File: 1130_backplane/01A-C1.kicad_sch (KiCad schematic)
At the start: 86 parts

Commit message: Removed power rails off 01A-C1 N2 connector
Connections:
- net +3V: no longer J253.b2 (Pin_b2)
- net +6V: no longer J253.a10 (Pin_a10)
- net -3V: no longer J253.a5 (Pin_a5)
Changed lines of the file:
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@@
     (stroke (width 0) (type solid) (color 0 0 0 0))
-  )
-  (wire (pts (xy 538.48 127) (xy 546.1 127))
-    (stroke (width 0) (type default) (color 0 0 0 0))
   )
   (wire (pts (xy 306.07 119.38) (xy 314.96 119.38))
@@
     (stroke (width 0) (type default) (color 0 0 0 0))
   )
-  (wire (pts (xy 558.8 106.68) (xy 566.42 106.68))
-    (stroke (width 0) (type default) (color 0 0 0 0))
-  )
   (polyline (pts (xy 196.85 33.02) (xy 198.12 33.02))
     (stroke (width 0) (type solid) (color 0 0 0 0))
@@
     (stroke (width 0) (type default) (color 0 0 0 0))
   )
-  (wire (pts (xy 538.48 114.3) (xy 546.1 114.3))
-    (stroke (width 0) (type default) (color 0 0 0 0))
-  )
   (wire (pts (xy 160.02 152.4) (xy 167.64 152.4))
     (stroke (width 0) (type default) (color 0 0 0 0))
@@
     (effects (font (size 1.27 1.27)) (justify right bottom))
   )
-  (label "-3V" (at 538.48 114.3 180)
-    (effects (font (size 1.27 1.27)) (justify right bottom))
-  )
   (label "+3V" (at 440.69 144.78 0)
     (effects (font (size 1.27 1.27)) (justify left bottom))
@@
     (effects (font (size 1.27 1.27)) (justify right bottom))
   )
-  (label "+3V" (at 566.42 106.68 0)
-    (effects (font (size 1.27 1.27)) (justify left bottom))
-  )
   (label "+3V" (at 482.6 182.88 0)
     (effects (font (size 1.27 1.27)) (justify left bottom))
@@
     (effects (font (size 1.27 1.27)) (justify left bottom))
   )
-  (label "+6V" (at 538.48 127 180)
-    (effects (font (size 1.27 1.27)) (justify right bottom))
-  )
   (label "-3V" (at 160.02 266.7 180)

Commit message: DN101-DN111 added to backplane schematics, DN111 01B-A1 connections made, 01B-B1 connections to be made when all signals on connectors
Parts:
- removed J173, J174, J175, J176, J177, J178, J179, J180, J181, J182, J183, J184, J185, J186, J187, J188, J189, J190, J191, J192, J193, J194, J195, J196, J197, J198, J199, J200, J201, J202, J203, J204, J205, J206, J207, J208, J209, J210, J211, J212, J213, J214, J215, J216, J217, J218, J219, J220, J221, J222, J223, J224, J225, J226, J227, J228, J229, J230, J231, J232, J233, J234, J235, J236, J237, J238, J239, J240, J241, J242, J243, J244, J245, J246, J247, J248, J249, J250, J251, J252, J253, J254, J255, J256, J257, J258: ~, symbol Connector_Generic:Conn_02x12_Row_Letter_First
- added J? (x86): ~, symbol Connector_Generic:Conn_02x12_Row_Letter_First
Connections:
- net +3V: now also J?.b2 (Pin_b2), J?.b2 (Pin_b2), J?.b2 (Pin_b2), J?.b2 (Pin_b2), J?.b2 (Pin_b2), J?.b2 (Pin_b2), J?.b2 (Pin_b2), J?.b2 (Pin_b2), J?.b2 (Pin_b2), J?.b2 (Pin_b2), J?.b2 (Pin_b2), J?.b2 (Pin_b2), J?.b2 (Pin_b2), J?.b2 (Pin_b2), J?.b2 (Pin_b2), J?.b2 (Pin_b2), J?.b2 (Pin_b2), J?.b2 (Pin_b2), J?.b2 (Pin_b2), J?.b2 (Pin_b2), J?.b2 (Pin_b2), J?.b2 (Pin_b2), J?.b2 (Pin_b2), J?.b2 (Pin_b2), J?.b2 (Pin_b2), J?.b2 (Pin_b2), J?.b2 (Pin_b2), J?.b2 (Pin_b2), J?.b2 (Pin_b2), J?.b2 (Pin_b2), J?.b2 (Pin_b2), J?.b2 (Pin_b2), J?.b2 (Pin_b2), J?.b2 (Pin_b2), J?.b2 (Pin_b2), J?.b2 (Pin_b2), J?.b2 (Pin_b2), J?.b2 (Pin_b2), J?.b2 (Pin_b2), J?.b2 (Pin_b2), J?.b2 (Pin_b2), J?.b2 (Pin_b2), J?.b2 (Pin_b2), J?.b2 (Pin_b2), J?.b2 (Pin_b2), J?.b2 (Pin_b2), J?.b2 (Pin_b2), J?.b2 (Pin_b2), J?.b2 (Pin_b2), J?.b2 (Pin_b2), J?.b2 (Pin_b2), J?.b2 (Pin_b2), J?.b2 (Pin_b2), J?.b2 (Pin_b2), J?.b2 (Pin_b2), J?.b2 (Pin_b2), J?.b2 (Pin_b2), J?.b2 (Pin_b2), J?.b2 (Pin_b2), J?.b2 (Pin_b2), J?.b2 (Pin_b2), J?.b2 (Pin_b2), J?.b2 (Pin_b2), J?.b2 (Pin_b2), J?.b2 (Pin_b2), J?.b2 (Pin_b2), J?.b2 (Pin_b2), J?.b2 (Pin_b2), J?.b2 (Pin_b2), J?.b2 (Pin_b2), J?.b2 (Pin_b2), J?.b2 (Pin_b2), J?.b2 (Pin_b2), J?.b2 (Pin_b2), J?.b2 (Pin_b2), J?.b2 (Pin_b2), J?.b2 (Pin_b2)
- net +6V: now also J?.a10 (Pin_a10), J?.a10 (Pin_a10), J?.a10 (Pin_a10), J?.a10 (Pin_a10), J?.a10 (Pin_a10), J?.a10 (Pin_a10), J?.a10 (Pin_a10), J?.a10 (Pin_a10), J?.a10 (Pin_a10), J?.a10 (Pin_a10), J?.a10 (Pin_a10), J?.a10 (Pin_a10), J?.a10 (Pin_a10), J?.a10 (Pin_a10), J?.a10 (Pin_a10), J?.a10 (Pin_a10), J?.a10 (Pin_a10), J?.a10 (Pin_a10), J?.a10 (Pin_a10), J?.a10 (Pin_a10), J?.a10 (Pin_a10), J?.a10 (Pin_a10), J?.a10 (Pin_a10), J?.a10 (Pin_a10), J?.a10 (Pin_a10), J?.a10 (Pin_a10), J?.a10 (Pin_a10), J?.a10 (Pin_a10), J?.a10 (Pin_a10), J?.a10 (Pin_a10), J?.a10 (Pin_a10), J?.a10 (Pin_a10), J?.a10 (Pin_a10), J?.a10 (Pin_a10), J?.a10 (Pin_a10), J?.a10 (Pin_a10), J?.a10 (Pin_a10), J?.a10 (Pin_a10), J?.a10 (Pin_a10), J?.a10 (Pin_a10), J?.a10 (Pin_a10), J?.a10 (Pin_a10), J?.a10 (Pin_a10), J?.a10 (Pin_a10), J?.a10 (Pin_a10), J?.a10 (Pin_a10), J?.a10 (Pin_a10), J?.a10 (Pin_a10), J?.a10 (Pin_a10), J?.a10 (Pin_a10), J?.a10 (Pin_a10), J?.a10 (Pin_a10), J?.a10 (Pin_a10), J?.a10 (Pin_a10), J?.a10 (Pin_a10), J?.a10 (Pin_a10), J?.a10 (Pin_a10), J?.a10 (Pin_a10), J?.a10 (Pin_a10), J?.a10 (Pin_a10), J?.a10 (Pin_a10), J?.a10 (Pin_a10), J?.a10 (Pin_a10), J?.a10 (Pin_a10), J?.a10 (Pin_a10), J?.a10 (Pin_a10), J?.a10 (Pin_a10), J?.a10 (Pin_a10), J?.a10 (Pin_a10), J?.a10 (Pin_a10), J?.a10 (Pin_a10), J?.a10 (Pin_a10), J?.a10 (Pin_a10), J?.a10 (Pin_a10), J?.a10 (Pin_a10), J?.a10 (Pin_a10), J?.a10 (Pin_a10)
- net -3V: now also J?.a5 (Pin_a5), J?.a5 (Pin_a5), J?.a5 (Pin_a5), J?.a5 (Pin_a5), J?.a5 (Pin_a5), J?.a5 (Pin_a5), J?.a5 (Pin_a5), J?.a5 (Pin_a5), J?.a5 (Pin_a5), J?.a5 (Pin_a5), J?.a5 (Pin_a5), J?.a5 (Pin_a5), J?.a5 (Pin_a5), J?.a5 (Pin_a5), J?.a5 (Pin_a5), J?.a5 (Pin_a5), J?.a5 (Pin_a5), J?.a5 (Pin_a5), J?.a5 (Pin_a5), J?.a5 (Pin_a5), J?.a5 (Pin_a5), J?.a5 (Pin_a5), J?.a5 (Pin_a5), J?.a5 (Pin_a5), J?.a5 (Pin_a5), J?.a5 (Pin_a5), J?.a5 (Pin_a5), J?.a5 (Pin_a5), J?.a5 (Pin_a5), J?.a5 (Pin_a5), J?.a5 (Pin_a5), J?.a5 (Pin_a5), J?.a5 (Pin_a5), J?.a5 (Pin_a5), J?.a5 (Pin_a5), J?.a5 (Pin_a5), J?.a5 (Pin_a5), J?.a5 (Pin_a5), J?.a5 (Pin_a5), J?.a5 (Pin_a5), J?.a5 (Pin_a5), J?.a5 (Pin_a5), J?.a5 (Pin_a5), J?.a5 (Pin_a5), J?.a5 (Pin_a5), J?.a5 (Pin_a5), J?.a5 (Pin_a5), J?.a5 (Pin_a5), J?.a5 (Pin_a5), J?.a5 (Pin_a5), J?.a5 (Pin_a5), J?.a5 (Pin_a5), J?.a5 (Pin_a5), J?.a5 (Pin_a5), J?.a5 (Pin_a5), J?.a5 (Pin_a5), J?.a5 (Pin_a5), J?.a5 (Pin_a5), J?.a5 (Pin_a5), J?.a5 (Pin_a5), J?.a5 (Pin_a5), J?.a5 (Pin_a5), J?.a5 (Pin_a5), J?.a5 (Pin_a5), J?.a5 (Pin_a5), J?.a5 (Pin_a5), J?.a5 (Pin_a5), J?.a5 (Pin_a5), J?.a5 (Pin_a5), J?.a5 (Pin_a5), J?.a5 (Pin_a5), J?.a5 (Pin_a5), J?.a5 (Pin_a5), J?.a5 (Pin_a5), J?.a5 (Pin_a5), J?.a5 (Pin_a5), J?.a5 (Pin_a5)
- net -IO_BIT_0: now also J?.a1 (Pin_a1), J?.a2 (Pin_a2)
- net -IO_BIT_1: now also J?.b1 (Pin_b1), J?.b1 (Pin_b1)
- net -IO_BIT_10: now also J?.a7 (Pin_a7), J?.a7 (Pin_a7)
- net -IO_BIT_11: now also J?.b6 (Pin_b6), J?.b8 (Pin_b8)
- net -IO_BIT_12: now also J?.a8 (Pin_a8), J?.a8 (Pin_a8)
- net -IO_BIT_13: now also J?.b8 (Pin_b8), J?.b9 (Pin_b9)
- net -IO_BIT_14: now also J?.a9 (Pin_a9), J?.a9 (Pin_a9)
- net -IO_BIT_15: now also J?.b10 (Pin_b10), J?.b9 (Pin_b9)
- net -IO_BIT_2: now also J?.a2 (Pin_a2), J?.a3 (Pin_a3)
- net -IO_BIT_3: now also J?.a1 (Pin_a1), J?.b2 (Pin_b2), J?.b3 (Pin_b3)
- net -IO_BIT_4: now also J?.a3 (Pin_a3), J?.a4 (Pin_a4)
- net -IO_BIT_5: now also J?.b3 (Pin_b3), J?.b4 (Pin_b4)
- net -IO_BIT_6: now also J?.a11 (Pin_a11), J?.a4 (Pin_a4), J?.a5 (Pin_a5)
- net -IO_BIT_7: now also J?.b4 (Pin_b4), J?.b5 (Pin_b5)
- net -IO_BIT_8: now also J?.a6 (Pin_a6), J?.a6 (Pin_a6)
- net -IO_BIT_9: now also J?.b5 (Pin_b5), J?.b6 (Pin_b6)
- net GND: now also J?.b7 (Pin_b7), J?.b7 (Pin_b7), J?.b7 (Pin_b7), J?.b7 (Pin_b7), J?.b7 (Pin_b7), J?.b7 (Pin_b7), J?.b7 (Pin_b7), J?.b7 (Pin_b7), J?.b7 (Pin_b7), J?.b7 (Pin_b7), J?.b7 (Pin_b7), J?.b7 (Pin_b7), J?.b7 (Pin_b7), J?.b7 (Pin_b7), J?.b7 (Pin_b7), J?.b7 (Pin_b7), J?.b7 (Pin_b7), J?.b7 (Pin_b7), J?.b7 (Pin_b7), J?.b7 (Pin_b7), J?.b7 (Pin_b7), J?.b7 (Pin_b7), J?.b7 (Pin_b7), J?.b7 (Pin_b7), J?.b7 (Pin_b7), J?.b7 (Pin_b7), J?.b7 (Pin_b7), J?.b7 (Pin_b7), J?.b7 (Pin_b7), J?.b7 (Pin_b7), J?.b7 (Pin_b7), J?.b7 (Pin_b7), J?.b7 (Pin_b7), J?.b7 (Pin_b7), J?.b7 (Pin_b7), J?.b7 (Pin_b7), J?.b7 (Pin_b7), J?.b7 (Pin_b7), J?.b7 (Pin_b7), J?.b7 (Pin_b7), J?.b7 (Pin_b7), J?.b7 (Pin_b7), J?.b7 (Pin_b7), J?.b7 (Pin_b7), J?.b7 (Pin_b7), J?.b7 (Pin_b7), J?.b7 (Pin_b7), J?.b7 (Pin_b7), J?.b7 (Pin_b7), J?.b7 (Pin_b7), J?.b7 (Pin_b7), J?.b7 (Pin_b7), J?.b7 (Pin_b7), J?.b7 (Pin_b7), J?.b7 (Pin_b7), J?.b7 (Pin_b7), J?.b7 (Pin_b7), J?.b7 (Pin_b7), J?.b7 (Pin_b7), J?.b7 (Pin_b7), J?.b7 (Pin_b7), J?.b7 (Pin_b7), J?.b7 (Pin_b7), J?.b7 (Pin_b7), J?.b7 (Pin_b7), J?.b7 (Pin_b7), J?.b7 (Pin_b7), J?.b7 (Pin_b7), J?.b7 (Pin_b7), J?.b7 (Pin_b7), J?.b7 (Pin_b7), J?.b7 (Pin_b7), J?.b7 (Pin_b7), J?.b7 (Pin_b7), J?.b7 (Pin_b7), J?.b7 (Pin_b7), J?.b7 (Pin_b7), J?.b7 (Pin_b7), J?.b7 (Pin_b7), J?.b7 (Pin_b7), J?.b7 (Pin_b7), J?.b7 (Pin_b7), J?.b7 (Pin_b7), J?.b7 (Pin_b7), J?.b7 (Pin_b7), J?.b7 (Pin_b7)

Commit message: Add labels for cable runs, completed tracing for DN111 from previous commit, decided it would be too much work to go back and route later... Completed DN201 page.
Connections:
- net +3V: no longer J?.b2 (Pin_b2), J?.b2 (Pin_b2), J?.b2 (Pin_b2)
- net +6V: no longer J?.a10 (Pin_a10), J?.a10 (Pin_a10), J?.a10 (Pin_a10)
- net -3V: no longer J?.a5 (Pin_a5), J?.a5 (Pin_a5), J?.a5 (Pin_a5)
- net +INT_RUN_MODE: now reaches J?.a4 (Pin_a4)
- net +INT_RUN_MODE: now also J?.a4 (Pin_a4), J?.b6 (Pin_b6)
- net -XIO_TIME_GATE: now reaches J?.a3 (Pin_a3)
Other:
- note added: "CABL 01A-B1T1"
- note added: "CABL 01B-A1A6"
- note added: "CABL 01B-A1A7"
- note added: "CABL 01B-B1N5"
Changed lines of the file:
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@@
     (stroke (width 0) (type solid) (color 0 0 0 0))
-  )
-  (wire (pts (xy 807.72 260.35) (xy 815.34 260.35))
-    (stroke (width 0) (type default) (color 0 0 0 0))
   )
   (wire (pts (xy 680.72 234.95) (xy 688.34 234.95))
@@
     (stroke (width 0) (type solid) (color 0 0 0 0))
   )
-  (wire (pts (xy 25.4 306.07) (xy 33.02 306.07))
-    (stroke (width 0) (type default) (color 0 0 0 0))
-  )
   (wire (pts (xy 744.22 184.15) (xy 751.84 184.15))
     (stroke (width 0) (type default) (color 0 0 0 0))
@@
     (stroke (width 0) (type default) (color 0 0 0 0))
   )
-  (wire (pts (xy 25.4 318.77) (xy 33.02 318.77))
-    (stroke (width 0) (type default) (color 0 0 0 0))
-  )
   (wire (pts (xy 426.72 234.95) (xy 434.34 234.95))
     (stroke (width 0) (type default) (color 0 0 0 0))
@@
     (stroke (width 0) (type solid) (color 0 0 0 0))
   )
-  (wire (pts (xy 787.4 191.77) (xy 795.02 191.77))
-    (stroke (width 0) (type default) (color 0 0 0 0))
-  )
-  (wire (pts (xy 45.72 298.45) (xy 53.34 298.45))
-    (stroke (width 0) (type default) (color 0 0 0 0))
-  )
   (wire (pts (xy 490.22 260.35) (xy 497.84 260.35))
     (stroke (width 0) (type default) (color 0 0 0 0))
@@
     (stroke (width 0) (type default) (color 0 0 0 0))
   )
-  (wire (pts (xy 787.4 204.47) (xy 795.02 204.47))
-    (stroke (width 0) (type default) (color 0 0 0 0))
-  )
   (wire (pts (xy 109.22 260.35) (xy 116.84 260.35))
     (stroke (width 0) (type default) (color 0 0 0 0))
@@
     (stroke (width 0) (type default) (color 0 0 0 0))
   )
-  (wire (pts (xy 787.4 280.67) (xy 795.02 280.67))
-    (stroke (width 0) (type default) (color 0 0 0 0))
-  )
   (wire (pts (xy 553.72 107.95) (xy 561.34 107.95))
     (stroke (width 0) (type default) (color 0 0 0 0))
@@
     (stroke (width 0) (type default) (color 0 0 0 0))
   )
-  (wire (pts (xy 807.72 184.15) (xy 815.34 184.15))
-    (stroke (width 0) (type default) (color 0 0 0 0))
-  )
   (polyline (pts (xy 330.2 30.48) (xy 330.2 29.21))
     (stroke (width 0) (type solid) (color 0 0 0 0))
@@
     (stroke (width 0) (type default) (color 0 0 0 0))
   )
-  (wire (pts (xy 787.4 267.97) (xy 795.02 267.97))
-    (stroke (width 0) (type default) (color 0 0 0 0))
-  )
   (wire (pts (xy 680.72 107.95) (xy 688.34 107.95))
     (stroke (width 0) (type default) (color 0 0 0 0))
@@
     (effects (font (size 5 5) (thickness 1) bold) (justify left bottom))
   )
+  (text "CABL 01A-B1T1" (at 355.6 25.4 0)
+    (effects (font (size 1.27 1.27)) (justify left bottom))
+  )
   (text "E" (at 314.96 27.94 0)
     (effects (font (size 1.27 1.27)) (justify left bottom))
@@
     (effects (font (size 5 5) (thickness 1) bold) (justify left bottom))
   )
+  (text "CABL 01B-A1A6" (at 793.75 179.07 0)
+    (effects (font (size 1.27 1.27)) (justify left bottom))
+  )
   (text "C" (at 309.88 39.37 0)
     (effects (font (size 1.27 1.27)) (justify left bottom))
@@
     (effects (font (size 1.27 1.27)) (justify left bottom))
   )
+  (text "CABL 01B-B1N5" (at 793.75 102.87 0)
+    (effects (font (size 1.27 1.27)) (justify left bottom))
+  )
   (text "A" (at 36.83 339.09 0)
     (effects (font (size 5 5) (thickness 1) bold) (justify left bottom))
@@
     (effects (font (size 1.27 1.27)) (justify left bottom))
   )
+  (text "CABL 01B-A1A7" (at 793.75 255.27 0)
+    (effects (font (size 1.27 1.27)) (justify left bottom))
+  )
   (text "A" (at 332.74 27.94 0)
     (effects (font (size 1.27 1.27)) (justify left bottom))
@@
     (effects (font (size 1.27 1.27)) (justify left bottom))
   )
-  (label "-3V" (at 787.4 191.77 180)
-    (effects (font (size 1.27 1.27)) (justify right bottom))
-  )
   (label "+6V" (at 88.9 242.57 180)
     (effects (font (size 1.27 1.27)) (justify right bottom))
@@
     (effects (font (size 1.27 1.27)) (justify right bottom))
   )
-  (label "-3V" (at 787.4 267.97 180)
-    (effects (font (size 1.27 1.27)) (justify right bottom))
-  )
   (label "-3V" (at 533.4 306.07 180)
     (effects (font (size 1.27 1.27)) (justify right bottom))
@@
     (effects (font (size 1.27 1.27)) (justify right bottom))
   )
+  (label "+INT_RUN_MODE" (at 795.02 265.43 180)
+    (effects (font (size 1.27 1.27)) (justify right bottom))
+  )
   (label "+3V" (at 561.34 107.95 0)
     (effects (font (size 1.27 1.27)) (justify left bottom))
@@
     (effects (font (size 1.27 1.27)) (justify left bottom))
   )
-  (label "+3V" (at 815.34 184.15 0)
-    (effects (font (size 1.27 1.27)) (justify left bottom))
-  )
   (label "+3V" (at 180.34 146.05 0)
     (effects (font (size 1.27 1.27)) (justify left bottom))
@@
     (effects (font (size 1.27 1.27)) (justify left bottom))
   )
-  (label "+3V" (at 53.34 298.45 0)
-    (effects (font (size 1.27 1.27)) (justify left bottom))
-  )
   (label "GND" (at 243.84 158.75 0)
     (effects (font (size 1.27 1.27)) (justify left bottom))
@@
     (effects (font (size 1.27 1.27)) (justify left bottom))
   )
+  (label "-XIO_TIME_GATE" (at 795.02 186.69 180)
+    (effects (font (size 1.27 1.27)) (justify right bottom))
+  )
   (label "-3V" (at 215.9 191.77 180)
     (effects (font (size 1.27 1.27)) (justify right bottom))
@@
     (effects (font (size 1.27 1.27)) (justify right bottom))
   )
-  (label "+3V" (at 815.34 260.35 0)
+  (label "+INT_RUN_MODE" (at 45.72 232.41 0)
     (effects (font (size 1.27 1.27)) (justify left bottom))
   )
@@
     (effects (font (size 1.27 1.27)) (justify left bottom))
   )
-  (label "-3V" (at 25.4 306.07 180)
-    (effects (font (size 1.27 1.27)) (justify right bottom))
-  )
   (label "GND" (at 751.84 120.65 0)
     (effects (font (size 1.27 1.27)) (justify left bottom))
@@
     (effects (font (size 1.27 1.27)) (justify left bottom))
   )
+  (label "+INT_RUN_MODE" (at 33.02 303.53 180)
+    (effects (font (size 1.27 1.27)) (justify right bottom))
+  )
   (label "-IO_BIT_15" (at 807.72 128.27 0)
     (effects (font (size 1.27 1.27)) (justify left bottom))
@@
     (effects (font (size 1.27 1.27)) (justify right bottom))
   )
-  (label "+6V" (at 787.4 204.47 180)
-    (effects (font (size 1.27 1.27)) (justify right bottom))
-  )
   (label "-IO_BIT_12" (at 795.02 123.19 180)
     (effects (font (size 1.27 1.27)) (justify right bottom))
@@
     (effects (font (size 1.27 1.27)) (justify left bottom))
   )
-  (label "+6V" (at 787.4 280.67 180)
-    (effects (font (size 1.27 1.27)) (justify right bottom))
-  )
   (label "-3V" (at 596.9 153.67 180)
     (effects (font (size 1.27 1.27)) (justify right bottom))
@@
     (effects (font (size 1.27 1.27)) (justify left bottom))
   )
-  (label "+6V" (at 25.4 318.77 180)
-    (effects (font (size 1.27 1.27)) (justify right bottom))
-  )
   (label "-3V" (at 152.4 153.67 180)

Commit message: Add labels for bottom T[x] connectors, finished page DU101.
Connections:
- net -XIO_TIME_GATE: now also J?.b11 (Pin_b11), J?.b6 (Pin_b6)
- net +XIO_READ: now reaches J?.b12 (Pin_b12)
- net +XIO_READ: now also J?.a3 (Pin_a3), J?.b3 (Pin_b3)
- net DU101_AN4: now reaches J?.b9 (Pin_b9)
- net DU101_AN4: now also J?.b6 (Pin_b6)
- net -U_BIT_9: now reaches J?.a12 (Pin_a12)
- net -U_BIT_8: now reaches J?.a4 (Pin_a4)
- net -U_BIT_7: now reaches J?.a7 (Pin_a7)
- net -U_BIT_7: now also J?.b9 (Pin_b9)
- net -U_BIT_5: now reaches J?.b11 (Pin_b11)
- net -U_BIT_5: now also J?.a9 (Pin_a9)
- net +U_REG_9_PWR: now reaches J?.b12 (Pin_b12)
- net +U_REG_9_PWR: now also J?.b9 (Pin_b9)
- net +U_REG_8_PWR: now reaches J?.b3 (Pin_b3)
- net +U_REG_8_PWR: now also J?.b8 (Pin_b8)
- net DU101_AJ4: now reaches J?.b6 (Pin_b6)
- net DU101_AJ4: now also J?.b10 (Pin_b10)
- net +U_REG_5_PWR: now reaches J?.b9 (Pin_b9)
- net +U_REG_5_PWR: now also J?.b11 (Pin_b11)
- net DU101_AD4: now reaches J?.a11 (Pin_a11)
- net DU101_AD4: now also J?.b12 (Pin_b12), J?.b12 (Pin_b12), J?.b9 (Pin_b9)
- net -U_BIT_6: now reaches J?.a12 (Pin_a12)
- net +XIO_TIME_GATE_AND_NOT_U6: now reaches J?.b11 (Pin_b11)
- net +XIO_TIME_GATE_AND_NOT_U6: now also J?.a6 (Pin_a6), J?.a7 (Pin_a7)
- net -PROGRAM_LOAD: now reaches J?.a8 (Pin_a8)
- net +ENTRY_GATE: now reaches J?.b4 (Pin_b4)
- net +ENTRY_GATE: now also J?.a4 (Pin_a4)
- net +AREA_4: now reaches J?.a2 (Pin_a2)
- net -XIO_START_READ_AND_AREA_4: now reaches J?.b3 (Pin_b3)
- net +XIO_START_READ: now reaches J?.b4 (Pin_b4)
- net +XIO_START_READ: now also J?.a12 (Pin_a12), J?.a4 (Pin_a4)
- net +XIO_CONTROL: now reaches J?.a1 (Pin_a1)
- net +XIO_CONTROL: now also J?.a5 (Pin_a5), J?.a8 (Pin_a8)
- net +XIO_WRITE: now reaches J?.b3 (Pin_b3)
- net +XIO_WRITE: now also J?.a6 (Pin_a6)
- net +XIO_START_WRITE: now reaches J?.b4 (Pin_b4)
- net +XIO_START_WRITE: now also J?.a3 (Pin_a3)
- net +XIO_SENSE_DEVICE: now reaches J?.b5 (Pin_b5)
- net +XIO_SENSE_DEVICE: now also J?.a11 (Pin_a11)
- net +XIO_SENSE_ILSW: now reaches J?.b6 (Pin_b6)
- net +XIO_SENSE_ILSW: now also J?.b5 (Pin_b5)
- net DU101_AU4: now reaches J?.a2 (Pin_a2)
- net DU101_AU4: now also J?.b6 (Pin_b6)
- net +LEVEL_0_DATA_GATE: now reaches J?.a4 (Pin_a4)
- net -C_S_LVL_0_PWR: now reaches J?.b1 (Pin_b1)
- net DU101_AV4: now reaches J?.b4 (Pin_b4)
- net DU101_AV4: now also J?.b8 (Pin_b8)
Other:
- note added: "5800000"
- note added: "5800236"
- note added: "5800533"
- note added: "5803016"
- note added: "5803421"
- note added: "5804008"
- note added: "CABL 01A-B1T2"
- moved on the sheet: J?

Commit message: Fix routing mistake from DU101 for T6, was 01A-A1 to 01A-B1, corrected from 01A-A1 to 01A-C1, finished page DU111.
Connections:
- net +AREA_4: now also J?.a3 (Pin_a3)
- net +XIO_SENSE_DEVICE: now also J?.b10 (Pin_b10)
- net +XIO_SENSE_ILSW: now also J?.a3 (Pin_a3)
- net DU111_AE4: now reaches J?.a11 (Pin_a11)
- net DU111_AE4: now also J?.b1 (Pin_b1)
- net DU111_AK4: now reaches J?.a12 (Pin_a12)
- net DU111_AK4: now also J?.b12 (Pin_b12)
- net DU111_AL4: now reaches J?.a9 (Pin_a9)
- net DU111_AL4: now also J?.a7 (Pin_a7)
- net DU111_AD4: now reaches J?.b12 (Pin_b12)
- net DU111_AD4: now also J?.a4 (Pin_a4), J?.b5 (Pin_b5)
- net -U_BIT_1: now reaches J?.a12 (Pin_a12)
- net -U_BIT_1: now also J?.a2 (Pin_a2)
- net DU111_BG4: now reaches J?.b12 (Pin_b12)
- net DU111_BG4: now also J?.a7 (Pin_a7)
- net -U_BIT_15: now reaches J?.a1 (Pin_a1)
- net -U_BIT_4: now reaches J?.a11 (Pin_a11)
- net -U_BIT_4: now also J?.a8 (Pin_a8), J?.b10 (Pin_b10)
- net -U_BIT_13: now reaches J?.a3 (Pin_a3)
- net -U_BIT_3: now reaches J?.a8 (Pin_a8)
- net -U_BIT_3: now also J?.b10 (Pin_b10), J?.b11 (Pin_b11)
- net -U_BIT_14: now reaches J?.a9 (Pin_a9)
- net +U_REG_15_PWR: now reaches J?.b1 (Pin_b1)
- net +U_REG_15_PWR: now also J?.a12 (Pin_a12), J?.b12 (Pin_b12)
- net DU111_AG4: now reaches J?.b10 (Pin_b10)
- net DU111_AG4: now also J?.b9 (Pin_b9)
- net +U_REG_14_PWR: now reaches J?.b4 (Pin_b4)
- net +U_REG_14_PWR: now also J?.b11 (Pin_b11), J?.b11 (Pin_b11)
- net +U_REG_13_PWR: now reaches J?.b5 (Pin_b5)
- net +U_REG_13_PWR: now also J?.b10 (Pin_b10)
- net DU111_AF4: now reaches J?.b8 (Pin_b8)
- net DU111_AF4: now also J?.a9 (Pin_a9)
- net +XIO_SENSE_RESET_15: now reaches J?.a1 (Pin_a1)
- net +XIO_SENSE_RESET_15: now also J?.a8 (Pin_a8)
- net +AREA_2: now reaches J?.a11 (Pin_a11)
- net +AREA_2: now also J?.a6 (Pin_a6), J?.b5 (Pin_b5)
- net -U_BIT_0: now reaches J?.a3 (Pin_a3)
- net -U_BIT_0: now also J?.a7 (Pin_a7), J?.b12 (Pin_b12)
- net -U_BIT_2: now reaches J?.a6 (Pin_a6)
- net -U_BIT_2: now also J?.b11 (Pin_b11)
- net -XIO_SENSE_RESET_14: now reaches J?.a9 (Pin_a9)
- net -XIO_SENSE_RESET_14: now also J?.a2 (Pin_a2)
- net +T6_PWR_2: now reaches J?.b12 (Pin_b12)
- net -XIO_SENSE_RESET_15: now reaches J?.b3 (Pin_b3)
- net -XIO_SENSE_RESET_15: now also J?.b9 (Pin_b9)
- net +AREA_8: now reaches J?.b3 (Pin_b3)
- net +AREA_8: now also J?.a11 (Pin_a11)
- net +AREA_6: now reaches J?.a11 (Pin_a11)
- net +AREA_6: now also J?.a6 (Pin_a6)
- net +AREA_3: now reaches J?.a7 (Pin_a7)
- net +AREA_3: now also J?.b3 (Pin_b3)
- net DU111_AV4: now reaches J?.a1 (Pin_a1)
- net DU111_AV4: now also J?.b1 (Pin_b1)
- net +AREA_1: now reaches J?.a12 (Pin_a12)
- net DU111_AT4: now reaches J?.a2 (Pin_a2)
- net DU111_AT4: now also J?.b6 (Pin_b6)
- net +AREA_7: now reaches J?.a4 (Pin_a4)
- net +AREA_5: now reaches J?.a8 (Pin_a8)
- net DU111_AU4: now reaches J?.b4 (Pin_b4)
- net DU111_AU4: now also J?.b8 (Pin_b8)
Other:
- note added: "5800509"
- note added: "5800716"
- note added: "CABL 01A-A1T6"

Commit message: Finish page KA101-KA111
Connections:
- net +PHASE_B: now reaches J?.b5 (Pin_b5)
- net +PHASE_B: now also J?.b11 (Pin_b11)
- net -DC_RESET_3: now reaches J?.a9 (Pin_a9)
- net -DC_RESET_3: now also J?.a9 (Pin_a9)
- net +RUN_PROG_LOAD_DOT_ON_RUN: now reaches J?.b6 (Pin_b6)
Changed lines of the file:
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@@
     (effects (font (size 1.27 1.27)) (justify right bottom))
+  )
+  (label "+RUN_PROG_LOAD_DOT_ON_RUN" (at 807.72 193.04 0)
+    (effects (font (size 1.27 1.27)) (justify left bottom))
   )
   (label "DU101_AD4" (at 414.02 243.84 180)
@@
     (effects (font (size 1.27 1.27)) (justify right bottom))
   )
+  (label "-DC_RESET_3" (at 795.02 200.66 180)
+    (effects (font (size 1.27 1.27)) (justify right bottom))
+  )
   (label "+6V" (at 469.9 165.1 180)
     (effects (font (size 1.27 1.27)) (justify right bottom))
@@
     (effects (font (size 1.27 1.27)) (justify right bottom))
   )
+  (label "+PHASE_B" (at 807.72 266.7 0)
+    (effects (font (size 1.27 1.27)) (justify left bottom))
+  )
   (label "+3V" (at 624.84 144.78 0)
     (effects (font (size 1.27 1.27)) (justify left bottom))
@@
     (effects (font (size 1.27 1.27)) (justify left bottom))
   )
+  (label "-DC_RESET_3" (at 33.02 314.96 180)
+    (effects (font (size 1.27 1.27)) (justify right bottom))
+  )
   (label "GND" (at 815.34 309.88 0)
     (effects (font (size 1.27 1.27)) (justify left bottom))
@@
     (effects (font (size 1.27 1.27)) (justify right bottom))
   )
+  (label "+PHASE_B" (at 45.72 320.04 0)
+    (effects (font (size 1.27 1.27)) (justify left bottom))
+  )
   (label "+6V" (at 469.9 241.3 180)

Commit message: Redo annotations...
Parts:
- gave numbers to parts that had none: 86

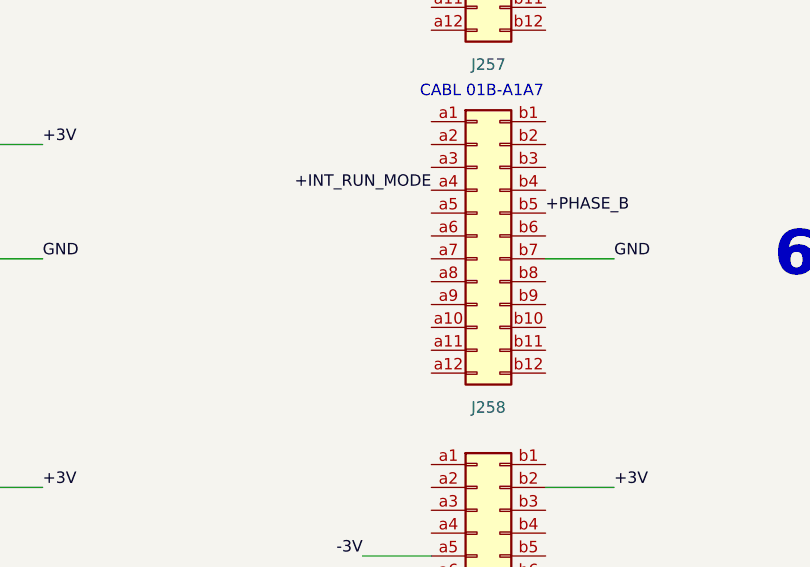
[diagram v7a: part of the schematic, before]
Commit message: Finish page KM101-KM111
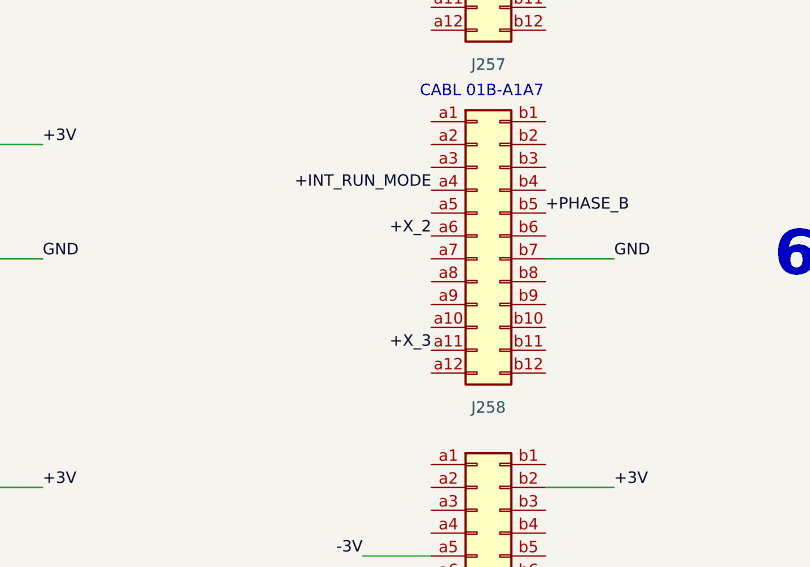
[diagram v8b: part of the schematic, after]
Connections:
- net +X_3: now reaches J257.a11 (Pin_a11)
- net +X_2: now reaches J257.a6 (Pin_a6)
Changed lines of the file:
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@@
     (effects (font (size 1.27 1.27)) (justify left bottom))
+  )
+  (label "+X_3" (at 795.02 281.94 180)
+    (effects (font (size 1.27 1.27)) (justify right bottom))
   )
   (label "+3V" (at 307.34 259.08 0)
@@
     (effects (font (size 1.27 1.27)) (justify right bottom))
   )
+  (label "+X_2" (at 795.02 269.24 180)
+    (effects (font (size 1.27 1.27)) (justify right bottom))
+  )
